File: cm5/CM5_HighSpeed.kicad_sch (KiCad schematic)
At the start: 9 parts, among them J5 USB3_A, J7 Conn_01x04, U6 AP22653W6

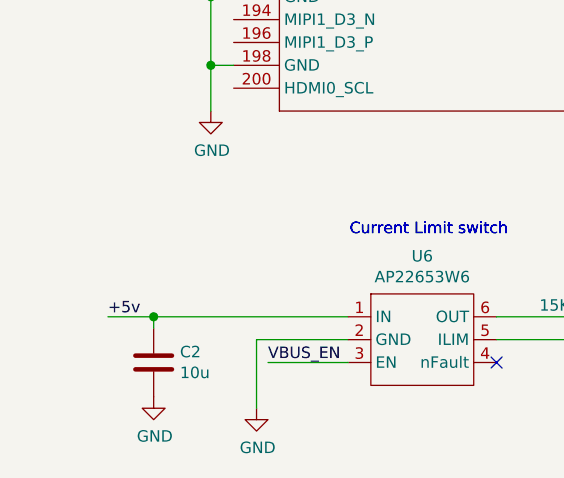
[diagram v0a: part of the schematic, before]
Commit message: PCM1863 switchover (#5)
* Oops, basically brand new ADC design using a new chip

* Working PCB and working driver, sort of

* --amend
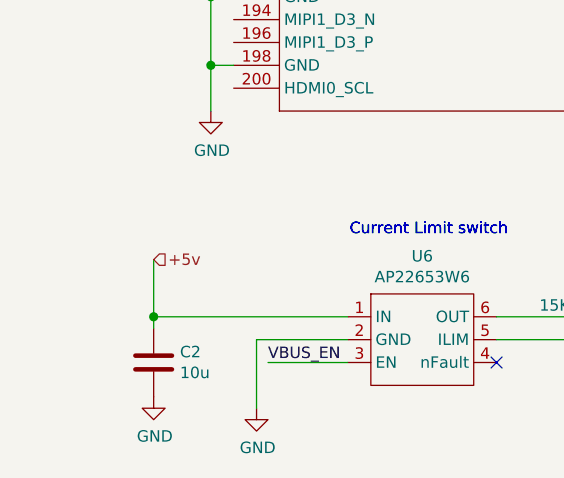
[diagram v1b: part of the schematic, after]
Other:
- company: E-SMART SOLUTIONS -> Ridgeline Radio
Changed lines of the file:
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@@
 		(title "Compute Module 5 IO ")
 		(rev "1")
-		(company "E-SMART SOLUTIONS")
-		(comment 1 "Mostafa Bakir")
+		(company "Ridgeline Radio")
+		(comment 1 "Jake Wood")
 	)
 	(text "Current Limit switch"
@@
 	(wire
 		(pts
-			(xy 24.13 175.26) (xy 29.21 175.26)
+			(xy 29.21 168.91) (xy 29.21 175.26)
 		)
 		(stroke
@@
 	(label "USB3-1-TX_P"
 		(at 102.87 114.3 0)
-		(effects
-			(font
-				(size 1.27 1.27)
-			)
-			(justify left bottom)
-		)
-	)
-	(label "+5v"
-		(at 24.13 175.26 0)
 		(effects
 			(font
@@
 		(effects
 			(font
+				(size 1.27 1.27)
+			)
+			(justify left)
+		)
+	)
+	(hierarchical_label "+5v"
+		(shape input)
+		(at 29.21 168.91 0)
+		(effects
+			(font

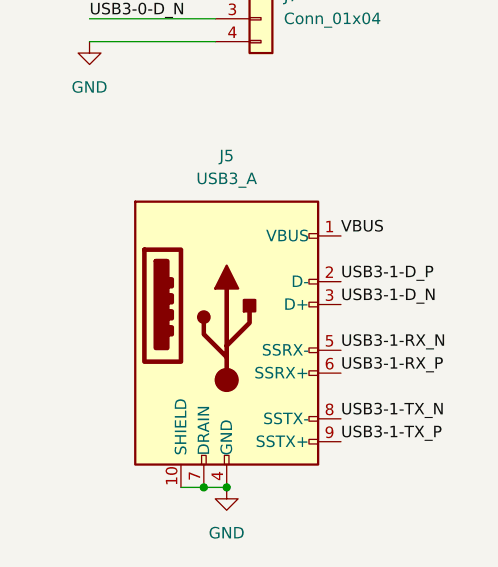
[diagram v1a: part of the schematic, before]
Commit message: Fix the usb port (just in case) #1
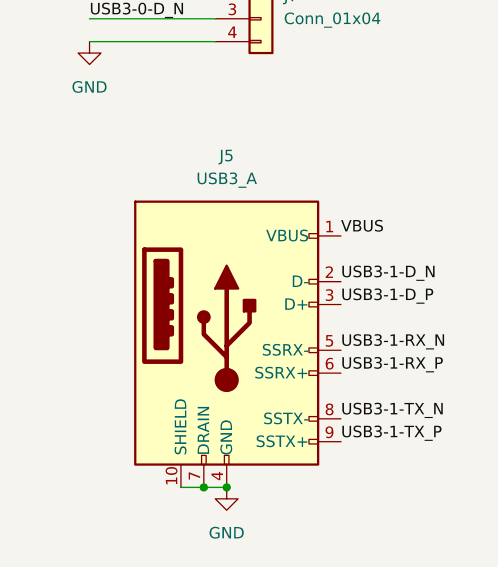
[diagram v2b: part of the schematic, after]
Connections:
- net USB3-1-D_N: now also J5.2 (D-); no longer J5.3 (D+)
- net USB3-1-D_P: now also J5.3 (D+); no longer J5.2 (D-)
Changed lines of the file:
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@@
 		)
 	)
-	(label "USB3-1-D_P"
+	(label "USB3-1-D_N"
 		(at 163.83 83.82 0)
 		(effects
@@
 		)
 	)
-	(label "USB3-1-D_N"
+	(label "USB3-1-D_P"
 		(at 163.83 86.36 0)
 		(effects

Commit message: Getting started on StudioHub adapter
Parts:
- removed J5: USB3_A, Connector_USB:C168717, symbol Connector:USB3_A
- J7: value Conn_01x04 -> Display
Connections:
- net USB3-1-D_N: no longer names the net of Module1.165 (USB3-1-D_N)
- net USB3-1-D_P: no longer names the net of Module1.163 (USB3-1-D_P)
- net USB3-1-RX_N: no longer names the net of Module1.157 (USB3-1-RX_N)
- net USB3-1-RX_P: no longer names the net of Module1.159 (USB3-1-RX_P)
- net USB3-1-TX_N: no longer names the net of Module1.169 (USB3-1-TX_N)
- net USB3-1-TX_P: no longer names the net of Module1.171 (USB3-1-TX_P)
